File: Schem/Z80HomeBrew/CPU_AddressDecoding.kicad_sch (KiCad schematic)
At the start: 18 parts, among them U10 ATF22V10C-10PU, U11 74HC273, U6 AS7C4096A-12TCN, U7 ATF22V10C-10PU, U8 Z084000xP, U9 SST39SF040-70-4C-PHE

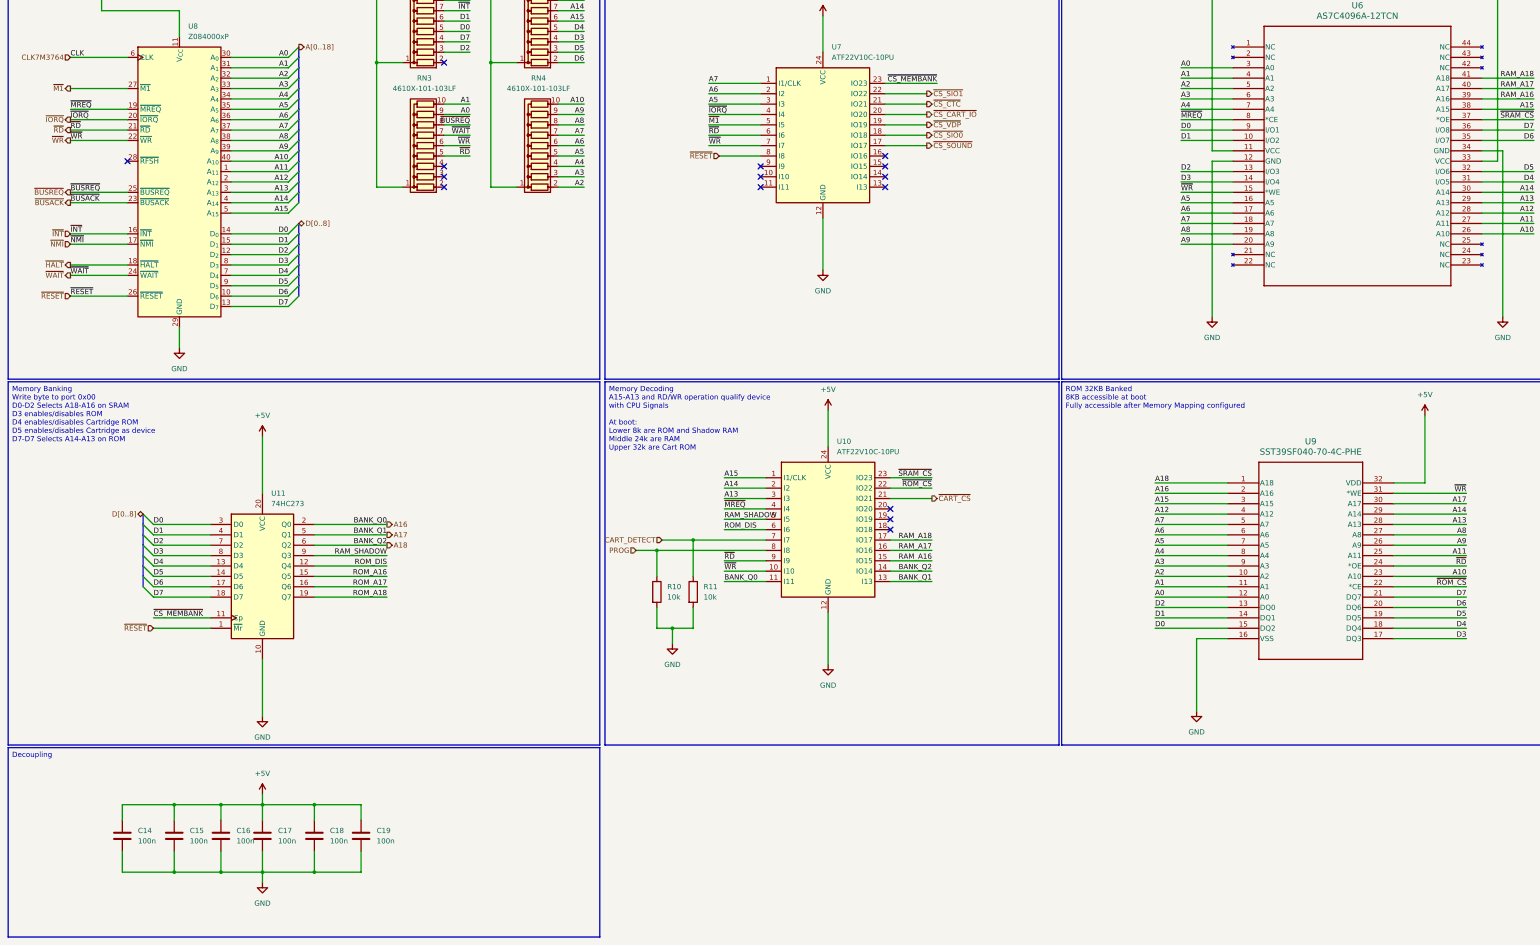
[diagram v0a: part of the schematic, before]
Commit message: Added the ability to read from the banking registers via IN instructions.
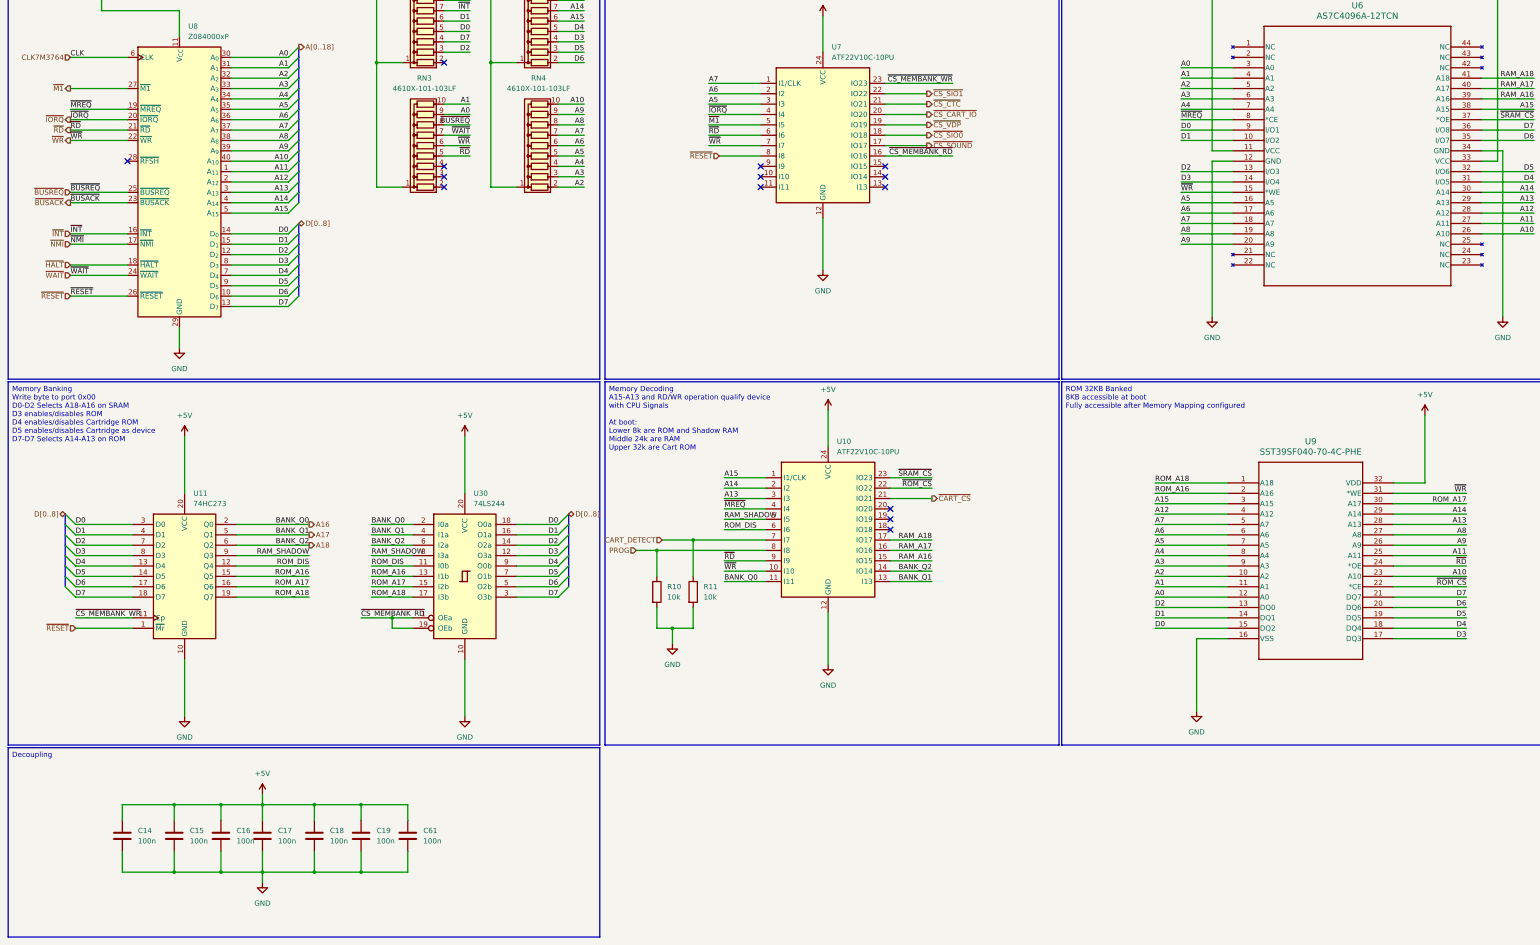
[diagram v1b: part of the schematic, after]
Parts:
- added C61: 100n, Capacitor_SMD:C_0805_2012Metric, symbol Device:C
- added U30: 74LS244, symbol 74xx:74LS244
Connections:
- net +5V: now also C61.1, U30.20 (VCC)
- net A16: now also U30.2 (I0a); no longer U9.2 (A16)
- net A17: now also U30.4 (I1a); no longer U9.30 (A17)
- net A18: now also U30.6 (I2a); no longer U9.1 (A18)
- net D0: now also U30.18 (O0a)
- net D1: now also U30.16 (O1a)
- net D2: now also U30.14 (O2a)
- net D3: now also U30.12 (O3a)
- net D4: now also U30.9 (O0b)
- net D5: now also U30.7 (O1b)
- net D6: now also U30.5 (O2b)
- net D7: now also U30.3 (O3b)
- net GND: now also C61.2, U30.10 (GND)
- net RAM_SHADOW: now also U30.8 (I3a)
- net ROM_A16: now also U9.2 (A16), U30.13 (I1b)
- net ROM_A17: now also U9.30 (A17), U30.15 (I2b)
- net ROM_A18: now also U9.1 (A18), U30.17 (I3b)
- net ROM_DIS: now also U30.11 (I0b)
- net ~{CS_MEMBANK_RD}: now reaches U7.16 (IO16)
- net ~{CS_MEMBANK_RD}: now also U30.1 (OEa), U30.19 (OEb)
- net ~{CS_MEMBANK} renamed ~{CS_MEMBANK_WR}
- no-connect marks 15 -> 14
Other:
- moved on the sheet: U11
